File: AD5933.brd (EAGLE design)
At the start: 82.8 x 53.3 mm, 80 parts, among them U1 ADG1604BRUZ, U10 ADP3303ARZ-3.3, U11 AD5242BRZ1M, U12 AD5245BRJZ100-R2, U2 AD5933YRSZ, U3 AD5242BRZ1M, U4 AD8606ARZ, U5 ADG1604BRUZ, U7 AD8606ARZ, U8 LTC6904MPMS8TRPBF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

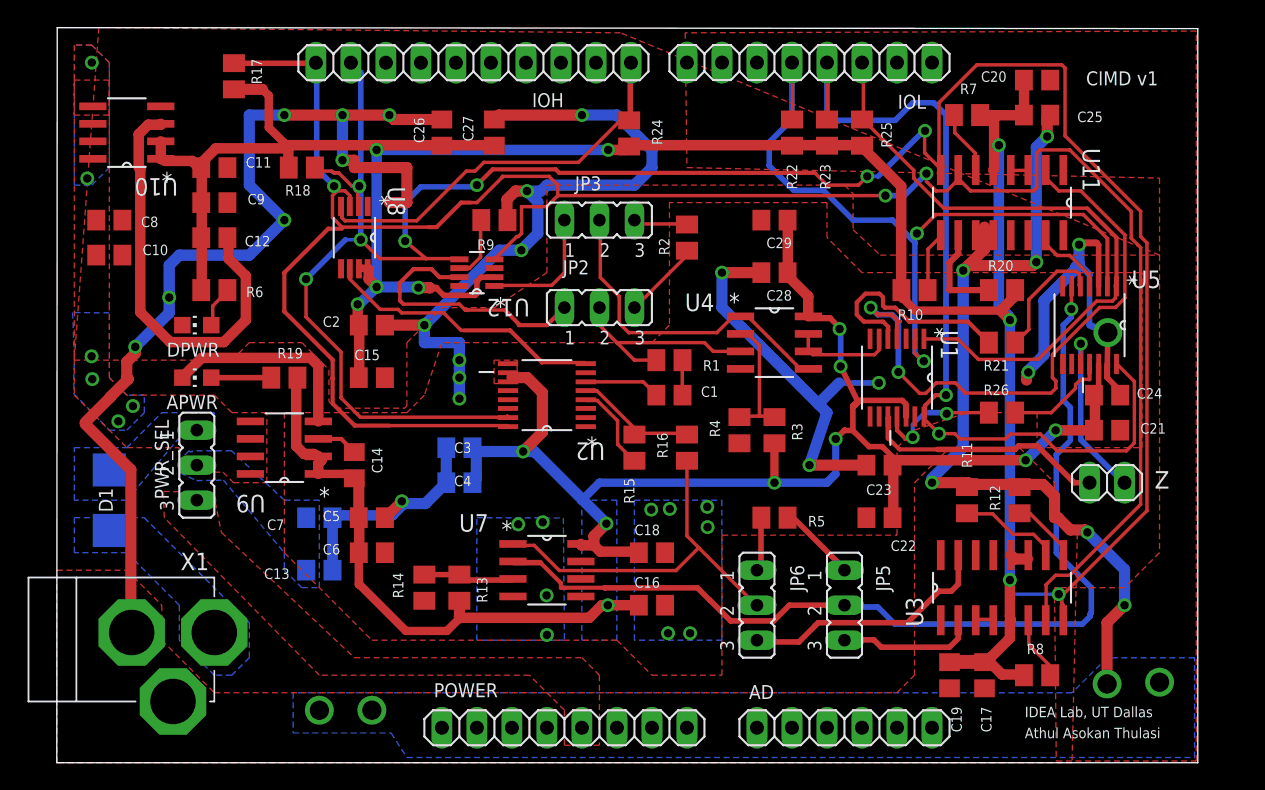
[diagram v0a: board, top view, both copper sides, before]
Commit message: Modified Silk screen
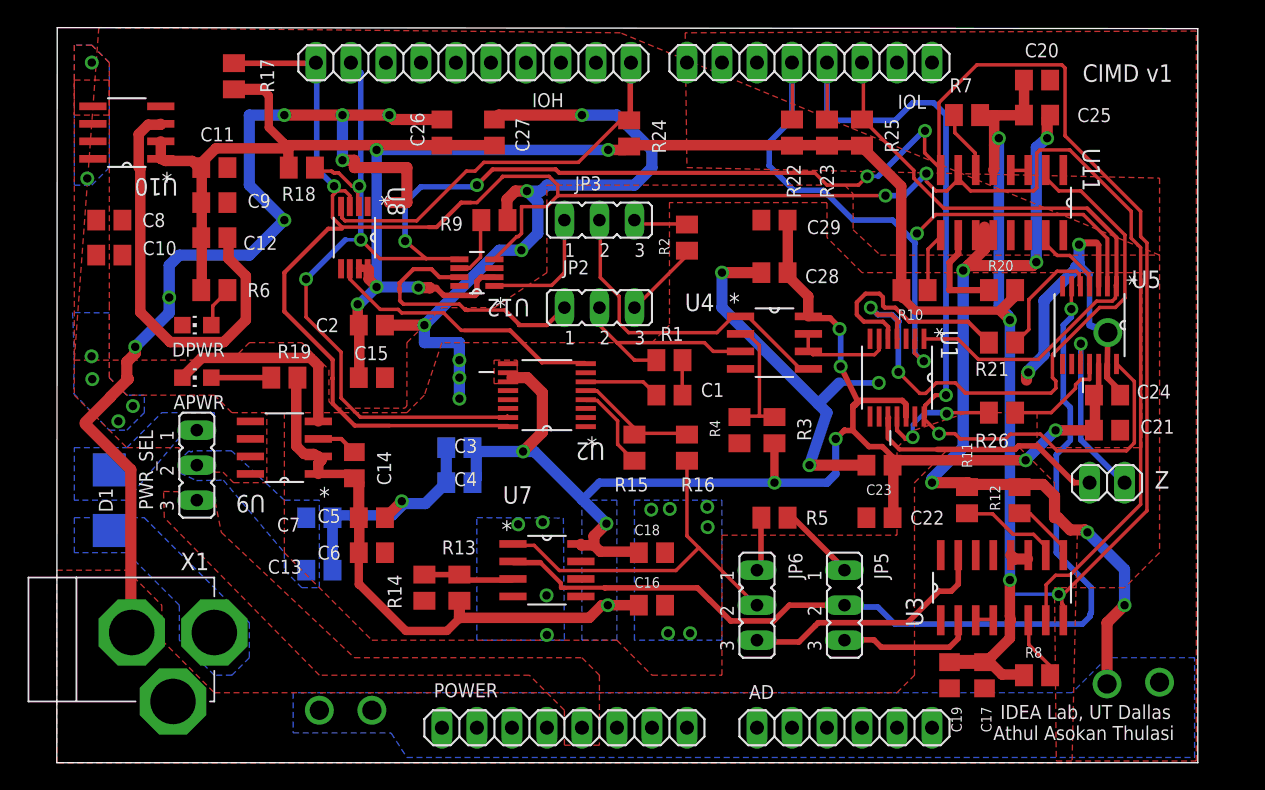
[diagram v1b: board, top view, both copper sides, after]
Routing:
- net VDD: track 187.1 -> 187.8 mm
